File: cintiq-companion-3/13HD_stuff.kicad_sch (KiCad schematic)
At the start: 22 parts, among them CN1 13HD_fingerpanel, J2 13HD_buttonboard, X1 13HD_eDP, X2 13HD_penpanel

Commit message: Did some footprint assignments and added reference image to pcb editor
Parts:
- C1, C2, C3, C4, C5, C6: footprint (none) -> Capacitor_SMD:C_0402_1005Metric
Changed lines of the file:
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@@
 			)
 		)
-		(property "Footprint" ""
+		(property "Footprint" "Capacitor_SMD:C_0402_1005Metric"
 			(at 233.68 36.83 0)
 			(effects
@@
 			)
 		)
-		(property "Footprint" ""
+		(property "Footprint" "Capacitor_SMD:C_0402_1005Metric"
 			(at 233.68 39.37 0)
 			(effects
@@
 			)
 		)
-		(property "Footprint" ""
+		(property "Footprint" "Capacitor_SMD:C_0402_1005Metric"
 			(at 233.68 46.99 0)
 			(effects
@@
 			)
 		)
-		(property "Footprint" ""
+		(property "Footprint" "Capacitor_SMD:C_0402_1005Metric"
 			(at 233.68 52.07 0)
 			(effects
@@
 			)
 		)
-		(property "Footprint" ""
+		(property "Footprint" "Capacitor_SMD:C_0402_1005Metric"
 			(at 233.68 54.61 0)
 			(effects
@@
 			)
 		)
-		(property "Footprint" ""
+		(property "Footprint" "Capacitor_SMD:C_0402_1005Metric"
 			(at 233.68 44.45 0)
 			(effects

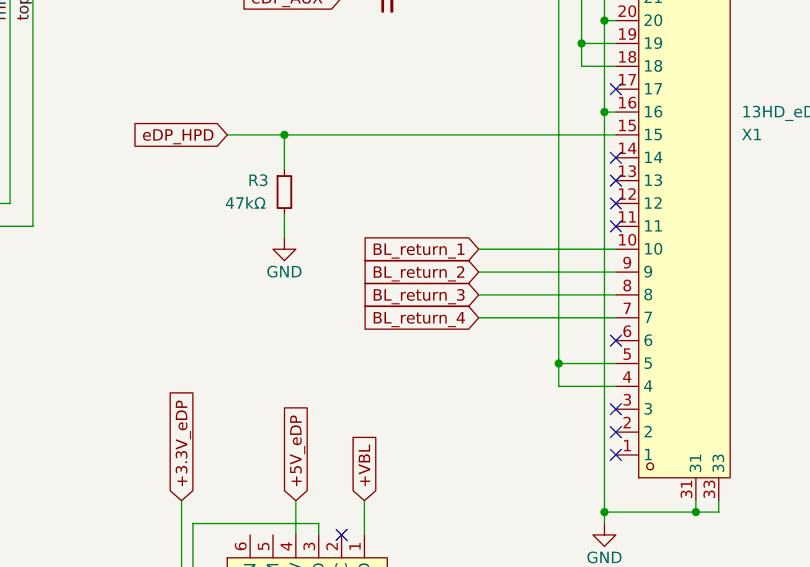
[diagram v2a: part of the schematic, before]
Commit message: Redid board outline according to reference and placed compute module slot
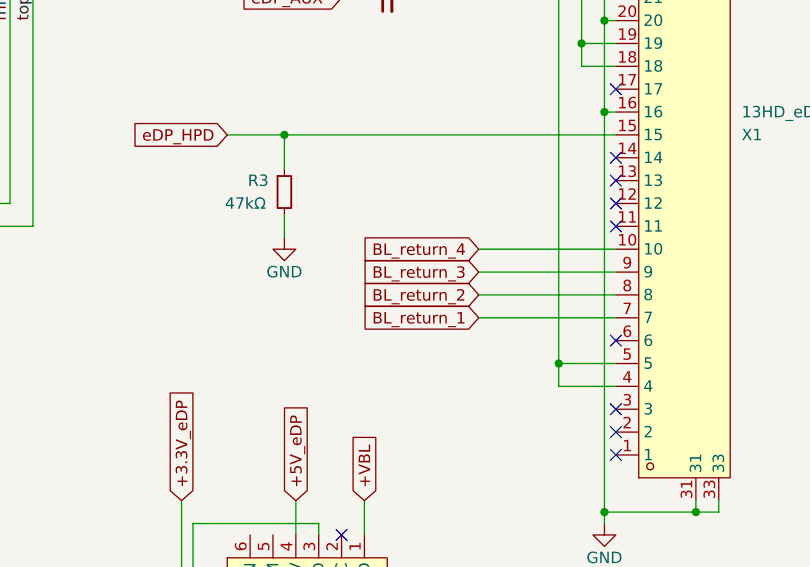
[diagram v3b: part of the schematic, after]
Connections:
- net BL_return_1: now also X1.7; no longer X1.10
- net BL_return_2: now also X1.8; no longer X1.9
- net BL_return_3: now also X1.9; no longer X1.8
- net BL_return_4: now also X1.10; no longer X1.7

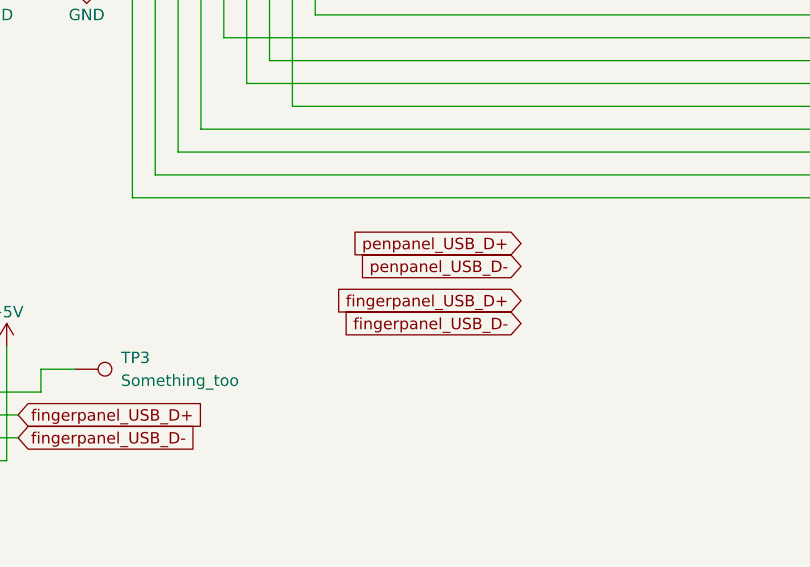
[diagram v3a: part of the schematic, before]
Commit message: Disconnected so far unused things on schematic
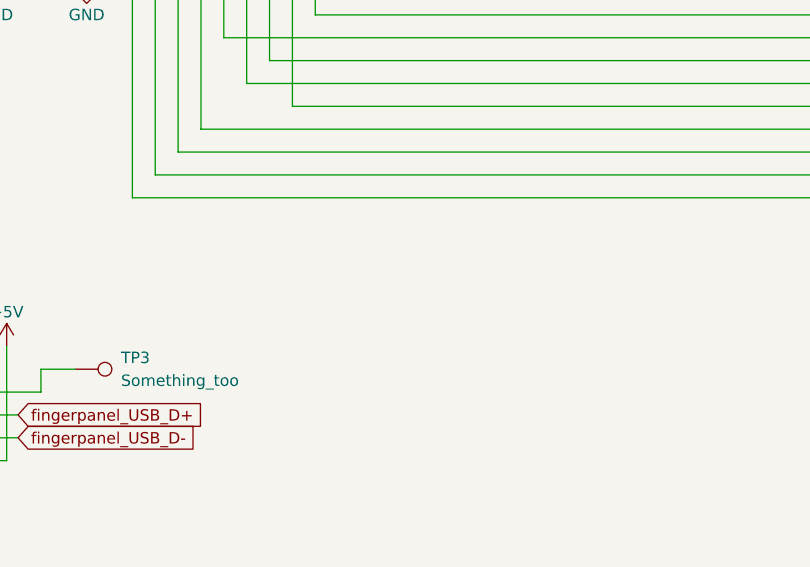
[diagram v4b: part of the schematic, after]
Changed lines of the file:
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@@
+		)
+	)
+	(global_label "+3.3V_eDP"
+		(shape input)
+		(at 210.82 110.49 90)
+		(fields_autoplaced yes)
+		(effects
+			(font
+				(size 1.27 1.27)
+			)
+			(justify left)
+		)
+		(property "Intersheetrefs" "${INTERSHEET_REFS}"
+			(at 210.82 97.2238 90)
+			(effects
+				(font
+					(size 1.27 1.27)
+				)
+				(justify left)
+				(hide yes)
+			)
+		)
+	)
+	(global_label "BL_return_4"
+		(shape input)
+		(at 226.06 149.86 270)
+		(fields_autoplaced yes)
+		(effects
+			(font
+				(size 1.27 1.27)
+			)
+			(justify right)
+		)
+		(property "Intersheetrefs" "${INTERSHEET_REFS}"
+			(at 226.06 163.9727 90)
+			(effects
+				(font
+					(size 1.27 1.27)
+				)
+				(justify right)
+				(hide yes)
+			)
+		)
+	)
+	(global_label "BL_return_2"
+		(shape input)
+		(at 243.84 87.63 180)
+		(fields_autoplaced yes)
+		(effects
+			(font
+				(size 1.27 1.27)
+			)
+			(justify right)
+		)
+		(property "Intersheetrefs" "${INTERSHEET_REFS}"
+			(at 229.7273 87.63 0)
+			(effects
+				(font
+					(size 1.27 1.27)
+				)
+				(justify right)
+				(hide yes)
+			)
+		)
+	)
+	(global_label "BL_return_1"
+		(shape input)
+		(at 243.84 90.17 180)
+		(fields_autoplaced yes)
+		(effects
+			(font
+				(size 1.27 1.27)
+			)
+			(justify right)
+		)
+		(property "Intersheetrefs" "${INTERSHEET_REFS}"
+			(at 229.7273 90.17 0)
+			(effects
+				(font
+					(size 1.27 1.27)
+				)
+				(justify right)
+				(hide yes)
+			)
+		)
+	)
+	(global_label "penpanel_USB_D+"
+		(shape input)
+		(at 102.87 38.1 270)
+		(fields_autoplaced yes)
+		(effects
+			(font
+				(size 1.27 1.27)
+			)
+			(justify right)
+		)
+		(property "Intersheetrefs" "${INTERSHEET_REFS}"
+			(at 102.87 58.2602 90)
+			(effects
+				(font
+					(size 1.27 1.27)
+				)
+				(justify right)
+				(hide yes)
+			)
+		)
+	)
+	(global_label "+5V_eDP"
+		(shape input)
+		(at 223.52 110.49 90)
+		(fields_autoplaced yes)
+		(effects
+			(font
+				(size 1.27 1.27)
+			)
+			(justify left)
+		)
+		(property "Intersheetrefs" "${INTERSHEET_REFS}"
+			(at 223.52 99.0381 90)
+			(effects
+				(font
+					(size 1.27 1.27)
+				)
+				(justify left)
+				(hide yes)
+			)
 		)
 	)
 	(global_label "fingerpanel_USB_D+"
 		(shape input)
-		(at 110.49 91.44 180)
-		(fields_autoplaced yes)
-		(effects
-			(font
-				(size 1.27 1.27)
-			)
-			(justify right)
-		)
-		(property "Intersheetrefs" "${INTERSHEET_REFS}"
-			(at 88.2131 91.44 0)
-			(effects
-				(font
-					(size 1.27 1.27)
-				)
-				(justify right)
-				(hide yes)
-			)
-		)
-	)
-	(global_label "+3.3V_eDP"
-		(shape input)
-		(at 210.82 110.49 90)
+		(at 54.61 104.14 0)
 		(fields_autoplaced yes)
 		(effects
@@
 		)
 		(property "Intersheetrefs" "${INTERSHEET_REFS}"
-			(at 210.82 97.2238 90)
+			(at 76.8869 104.14 0)
 			(effects
 				(font
@@
 		)
 	)
-	(global_label "BL_return_4"
-		(shape input)
-		(at 226.06 149.86 270)
-		(fields_autoplaced yes)
-		(effects
-			(font
-				(size 1.27 1.27)
-			)
-			(justify right)
-		)
-		(property "Intersheetrefs" "${INTERSHEET_REFS}"
-			(at 226.06 163.9727 90)
-			(effects
-				(font
-					(size 1.27 1.27)
-				)
-				(justify right)
-				(hide yes)
-			)
-		)
-	)
-	(global_label "BL_return_2"
-		(shape input)
-		(at 243.84 87.63 180)
-		(fields_autoplaced yes)
-		(effects
-			(font
-				(size 1.27 1.27)
-			)
-			(justify right)
-		)
-		(property "Intersheetrefs" "${INTERSHEET_REFS}"
-			(at 229.7273 87.63 0)
-			(effects
-				(font
-					(size 1.27 1.27)
-				)
-				(justify right)
-				(hide yes)
-			)
-		)
-	)
-	(global_label "BL_return_1"
-		(shape input)
-		(at 243.84 90.17 180)
-		(fields_autoplaced yes)
-		(effects
-			(font
-				(size 1.27 1.27)
-			)
-			(justify right)
-		)
-		(property "Intersheetrefs" "${INTERSHEET_REFS}"
-			(at 229.7273 90.17 0)
-			(effects
-				(font
-					(size 1.27 1.27)
-				)
-				(justify right)
-				(hide yes)
-			)
-		)
-	)
-	(global_label "penpanel_USB_D+"
-		(shape input)
-		(at 102.87 38.1 270)
-		(fields_autoplaced yes)
-		(effects
-			(font
-				(size 1.27 1.27)
-			)
-			(justify right)
-		)
-		(property "Intersheetrefs" "${INTERSHEET_REFS}"
-			(at 102.87 58.2602 90)
-			(effects
-				(font
-					(size 1.27 1.27)
-				)
-				(justify right)
-				(hide yes)
-			)
-		)
-	)
-	(global_label "+5V_eDP"
-		(shape input)
-		(at 223.52 110.49 90)
-		(fields_autoplaced yes)
-		(effects
-			(font
-				(size 1.27 1.27)
-			)
-			(justify left)
-		)
-		(property "Intersheetrefs" "${INTERSHEET_REFS}"
-			(at 223.52 99.0381 90)
-			(effects
-				(font
-					(size 1.27 1.27)
-				)
-				(justify left)
-				(hide yes)
-			)
-		)
-	)
-	(global_label "fingerpanel_USB_D+"
-		(shape input)
-		(at 54.61 104.14 0)
-		(fields_autoplaced yes)
-		(effects
-			(font
-				(size 1.27 1.27)
-			)
-			(justify left)
-		)
-		(property "Intersheetrefs" "${INTERSHEET_REFS}"
-			(at 76.8869 104.14 0)
-			(effects
-				(font
-					(size 1.27 1.27)
-				)
-				(justify left)
-				(hide yes)
-			)
-		)
-	)
 	(global_label "BL_return_3"
 		(shape input)
@@
 		)
 	)
-	(global_label "penpanel_USB_D+"
-		(shape input)
-		(at 110.49 85.09 180)
-		(fields_autoplaced yes)
-		(effects
-			(font
-				(size 1.27 1.27)
-			)
-			(justify right)
-		)
-		(property "Intersheetrefs" "${INTERSHEET_REFS}"
-			(at 90.3298 85.09 0)
-			(effects
-				(font
-					(size 1.27 1.27)
-				)
-				(justify right)
-				(hide yes)
-			)
-		)
-	)
 	(global_label "BL_return_3"
 		(shape input)
@@
 			(effects
 				(font
-					(size 1.27 1.27)
-				)
-				(justify right)
-				(hide yes)
-			)
-		)
-	)
-	(global_label "fingerpanel_USB_D-"
-		(shape input)
-		(at 110.49 93.98 180)
-		(fields_autoplaced yes)
-		(effects
-			(font
-				(size 1.27 1.27)
-			)
-			(justify right)
-		)
-		(property "Intersheetrefs" "${INTERSHEET_REFS}"
-			(at 90.3298 93.98 0)
-			(effects
-				(font
-					(size 1.27 1.27)
-				)
-				(justify right)
-				(hide yes)
-			)
-		)
-	)
-	(global_label "penpanel_USB_D-"
-		(shape input)
-		(at 110.49 87.63 180)
-		(fields_autoplaced yes)
-		(effects
-			(font
-				(size 1.27 1.27)
-			)
-			(justify right)
-		)
-		(property "Intersheetrefs" "${INTERSHEET_REFS}"
-			(at 90.3298 87.63 0)
-			(effects
-				(font

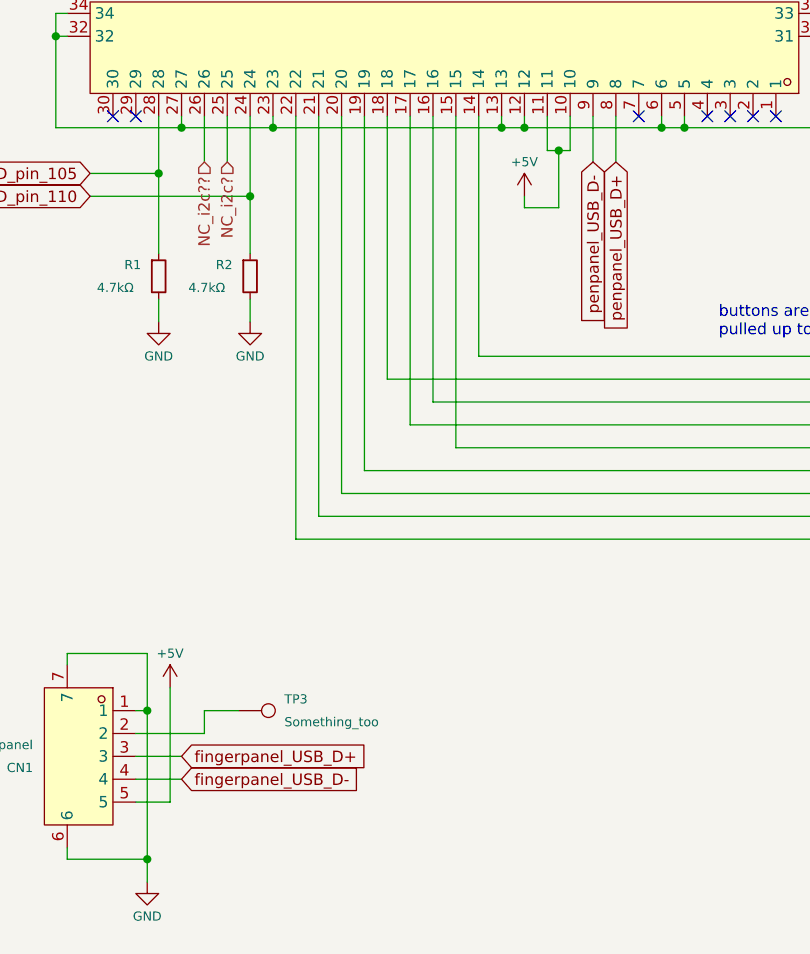
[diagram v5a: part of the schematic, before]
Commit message: routed usb
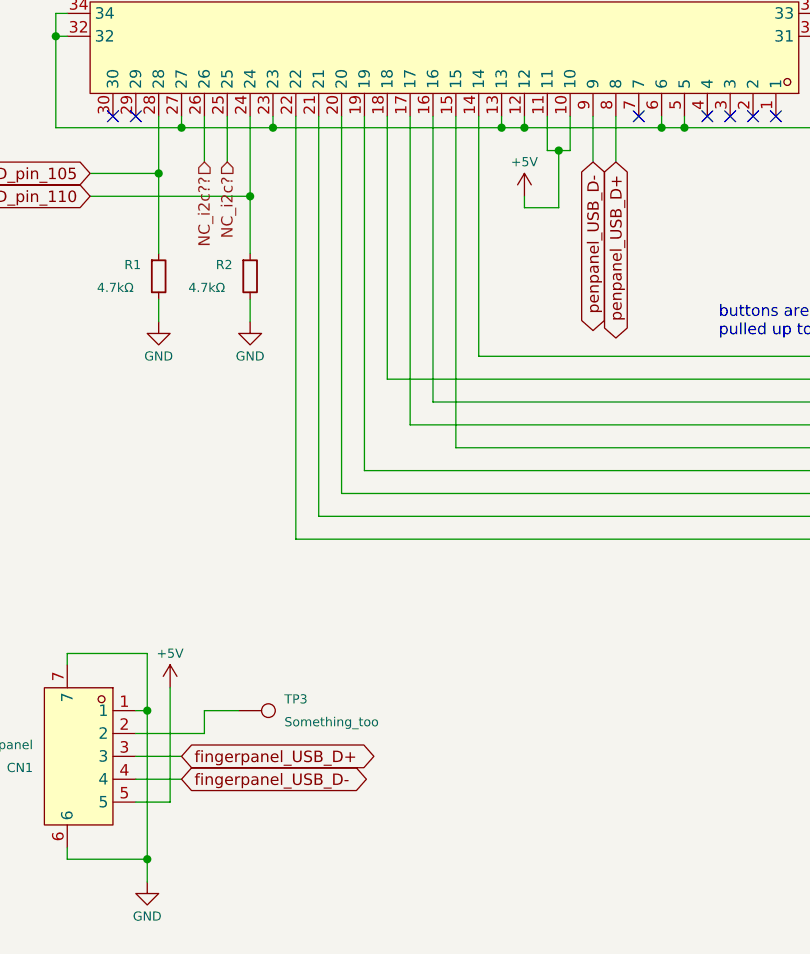
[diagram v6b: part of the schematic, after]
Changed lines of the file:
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@@
 	)
 	(global_label "penpanel_USB_D+"
-		(shape input)
+		(shape bidirectional)
 		(at 102.87 38.1 270)
 		(fields_autoplaced yes)
@@
 	)
 	(global_label "fingerpanel_USB_D+"
-		(shape input)
+		(shape bidirectional)
 		(at 54.61 104.14 0)
 		(fields_autoplaced yes)
@@
 	)
 	(global_label "penpanel_USB_D-"
-		(shape input)
+		(shape bidirectional)
 		(at 100.33 38.1 270)
 		(fields_autoplaced yes)
@@
 	)
 	(global_label "fingerpanel_USB_D-"
-		(shape input)
+		(shape bidirectional)
 		(at 54.61 106.68 0)
 		(fields_autoplaced yes)
